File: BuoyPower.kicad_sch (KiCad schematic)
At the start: 8 parts

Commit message: PiShield!!
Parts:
- removed H: MountingHole, symbol Mechanical:MountingHole
- removed J: Screw_Terminal_01x04, symbol Connector:Screw_Terminal_01x04
- added H (x2): MountingHole, symbol Mechanical:MountingHole
- added J: Conn_01x05, symbol Connector_Generic:Conn_01x05
- added J: Conn_01x03, symbol Connector_Generic:Conn_01x03
- added J (x2): Conn_01x04, symbol Connector_Generic:Conn_01x04
- added J: Conn_02x20_Odd_Even, symbol Connector_Generic:Conn_02x20_Odd_Even
- added J: Conn_01x02, symbol Connector_Generic:Conn_01x02
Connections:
- net +5V: now also J.1 (Pin_1), J.2 (Pin_2), J.2 (Pin_2), J.4 (Pin_4); no longer J.5 (Pin_5)
- net GND: now also J.2 (Pin_2), J.3 (Pin_3), J.1 (Pin_1), J.1 (Pin_1), J.3 (Pin_3), J.39 (Pin_39), J.4 (Pin_4), J.4 (Pin_4), J.6 (Pin_6)
- net PowerMonitor/VOUT: now also J.4 (Pin_4); no longer J.2 (Pin_2)
- net REG_EN: now also J.5 (Pin_5); no longer J.1 (Pin_1)
- net VBUS: now also J.1 (Pin_1), J.2 (Pin_2), J.5 (Pin_5); no longer J.2 (Pin_2)
- net +BATT renamed BATT_IN
- net BATT_IN: now also J.2 (Pin_2), J.1 (Pin_1), J.1 (Pin_1)
- removed net GND1: J.3 (Pin_3), J.4 (Pin_4)
- new net HOLD: J.1 (Pin_1), J.11 (Pin_11)
- new net SCL: J.2 (Pin_2), J.4 (Pin_4), J.5 (Pin_5)
- new net SDA: J.3 (Pin_3), J.3 (Pin_3), J.3 (Pin_3)
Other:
- sheet PowerTimer ports: added none; removed LATCH_CLEAR
- note added: "Battery In"
- note added: "Raspberry Pi In"
- note added: "Raspberry Pi Out"
- moved on the sheet: H, J

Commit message: Ready to order.
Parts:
- removed H: MountingHole, symbol Mechanical:MountingHole
- removed J: Conn_01x02, symbol Connector_Generic:Conn_01x02
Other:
- note added: "Qwiic Connector"
- note removed: "Battery In"
- note removed: "Raspberry Pi Out"
- moved on the sheet: H, J

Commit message: Post-build updates
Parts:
- removed H (x2): MountingHole, symbol Mechanical:MountingHole
- H: Mfr 1 (none) -> NA; Mfr 1 PN (none) -> NA; Supplier 1 Link (none) -> NA
- J: Mfr 1 (none) -> JST Sales America Inc.; Mfr 1 PN (none) -> S3B-XH-A; Supplier 1 Link (none) -> https://www.digikey.com/en/products/detail/jst-sales-americ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
- J: Mfr 1 (none) -> JST Sales America Inc.; Mfr 1 PN (none) -> S4B-XH-SM4-TB; Supplier 1 Link (none) -> https://www.digikey.com/en/products/detail/jst-sales-americ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
- J: Mfr 1 (none) -> Oupiin; Mfr 1 PN (none) -> 2047-2X20G00S3U; Supplier 1 Link (none) -> https://www.digikey.com/en/products/detail/oupiin/2047-2X20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
- J: Mfr 1 (none) -> Pololu; Mfr 1 PN (none) -> 3782; Supplier 1 Link (none) -> https://www.pololu.com/product/3782
- J: Mfr 1 (none) -> JST Sales America Inc.; Mfr 1 PN (none) -> S4B-XH-A; Supplier 1 Link (none) -> https://www.digikey.com/en/products/detail/jst-sales-americ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
- J: Mfr 1 (none) -> JST Sales America Inc.; Mfr 1 PN (none) -> S2B-XH-A; Supplier 1 Link (none) -> https://www.digikey.com/en/products/detail/jst-sales-americ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
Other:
- moved on the sheet: H

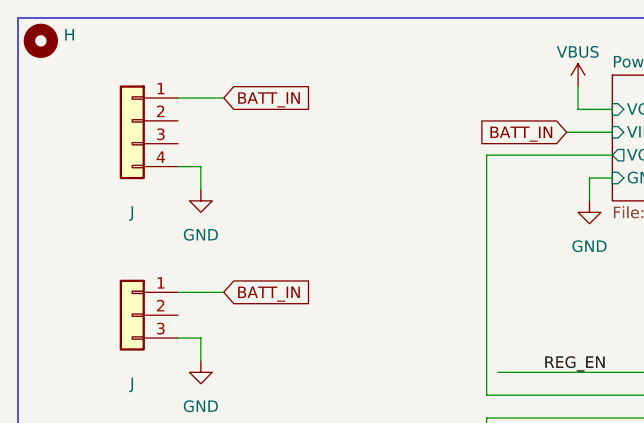
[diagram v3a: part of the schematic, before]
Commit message: revert to single layer
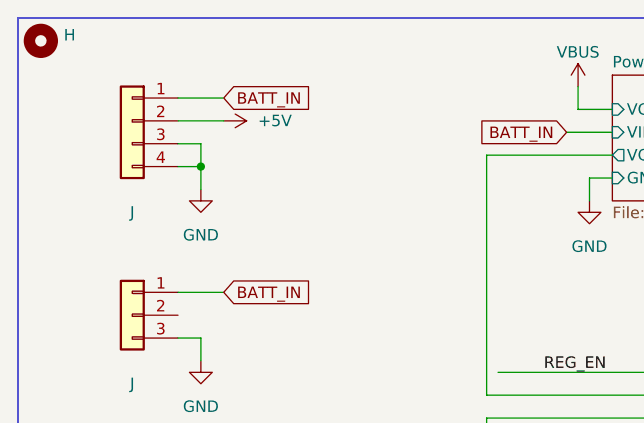
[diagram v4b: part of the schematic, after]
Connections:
- net +5V: now also J.2 (Pin_2)
- net GND: now also J.3 (Pin_3)
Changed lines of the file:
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@@
   (junction (at 106.68 100.33) (diameter 0) (color 0 0 0 0)
   )
+  (junction (at 74.93 69.85) (diameter 0) (color 0 0 0 0)
+  )
   (junction (at 198.12 73.66) (diameter 0) (color 0 0 0 0)
   )
@@
     (stroke (width 0) (type default))
   )
+  (wire (pts (xy 72.39 64.77) (xy 77.47 64.77))
+    (stroke (width 0) (type default))
+  )
   (wire (pts (xy 106.68 97.79) (xy 106.68 100.33))
     (stroke (width 0) (type default))
@@
     (stroke (width 0) (type default))
   )
+  (wire (pts (xy 74.93 67.31) (xy 74.93 69.85))
+    (stroke (width 0) (type default))
+  )
   (wire (pts (xy 190.5 73.66) (xy 198.12 73.66))
+    (stroke (width 0) (type default))
+  )
+  (wire (pts (xy 72.39 67.31) (xy 74.93 67.31))
     (stroke (width 0) (type default))
   )
@@
     )
     (property "Datasheet" "" (id 3) (at 231.14 114.3 0)
+      (effects (font (size 1.27 1.27)) hide)
+    )
+    (pin "1")
+  )
+  (symbol (lib_id "power:+5V") (at 77.47 64.77 270) (unit 1)
+    (in_bom yes) (on_board yes)
+    (default_instance (reference "#PWR") (unit 1) (value "+5V") (footprint ""))
+    (property "Reference" "#PWR" (id 0) (at 73.66 64.77 0)
+      (effects (font (size 1.27 1.27)) hide)
+    )
+    (property "Value" "+5V" (id 1) (at 81.28 64.77 90)
+      (effects (font (size 1.27 1.27)) (justify left))
+    )
+    (property "Footprint" "" (id 2) (at 77.47 64.77 0)
+      (effects (font (size 1.27 1.27)) hide)
+    )
+    (property "Datasheet" "" (id 3) (at 77.47 64.77 0)
       (effects (font (size 1.27 1.27)) hide)
     )
@@
       (reference "#PWR0117") (unit 1) (value "GND") (footprint "")
     )
+    (path "/76a9f0af-3f3f-49c0-897d-f2a243b75ef5"
+      (reference "#PWR0118") (unit 1) (value "+5V") (footprint "")
+    )
     (path "/1f46e0b0-8cf7-45e0-839e-129c08e67e35/f51e4d31-9573-41ba-83cc-77a97657d407"
       (reference "#PWR0119") (unit 1) (value "VBUS") (footprint "")
@@
       (reference "#PWR0120") (unit 1) (value "VBUS") (footprint "")
     )
-    (path "/76a9f0af-3f3f-49c0-897d-f2a243b75ef5"
+    (path "/38e8c5a9-e7df-42b5-8509-d128235845b3"
       (reference "#PWR0121") (unit 1) (value "+5V") (footprint "")
     )
@@
       (reference "S1") (unit 1) (value "EG1213") (footprint "EG1213:SW_EG1213")
     )
+    (path "/6d14d4f8-5eac-41fa-a6a0-78893e5397f9/8741732e-2853-4419-826c-b4fc8720471e"
+      (reference "U1") (unit 1) (value "74AHC1G02") (footprint "Package_TO_SOT_SMD:SOT-23-5_HandSoldering")
+    )
     (path "/1f46e0b0-8cf7-45e0-839e-129c08e67e35/4aca2538-caf6-445d-83c6-566769162211"
       (reference "U3") (unit 1) (value "INA219AxD") (footprint "Package_SO:SOIC-8_3.9x4.9mm_P1.27mm")
@@
       (reference "U9") (unit 1) (value "74AHC1GU04") (footprint "Package_TO_SOT_SMD:SOT-23-5_HandSoldering")
     )
-    (path "/6d14d4f8-5eac-41fa-a6a0-78893e5397f9/896736ad-6e08-4ccf-8ab3-eb5a87da7867"
-      (reference "U11") (unit 1) (value "SN74AHC1G32") (footprint "Package_TO_SOT_SMD:SOT-23-5_HandSoldering")
-    )
-  )
+  )
